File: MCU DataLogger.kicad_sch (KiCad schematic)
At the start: 0 parts

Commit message: Symbols added to first and second sheet
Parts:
- added BT1: Battery, symbol Device:Battery
- added C1, C2, C3, C4: C, symbol Device:C
- added C5: C_Polarized, symbol Device:C_Polarized
- added D1, D2: LED, symbol Device:LED
- added H1, H2, H3, H4: MountingHole, symbol Mechanical:MountingHole
- added R1, R2, R3, R4, R5, R6, R7: R, symbol Device:R
- added U1, U2: 24LC1025, symbol Memory_EEPROM:24LC1025
- added U3: DS1337S_, DS1337S_:SOIC127P600X175-8N, symbol DS1337S_:DS1337S_
- added U4: ATMEGA328P-AU, ATMEGA328P-AU:QFP80P900X900X120-32N, symbol ATMEGA328P-AU:ATMEGA328P-AU
- added Y1: Crystal, symbol Device:Crystal
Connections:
- new net GND: U4.21 (GND), U4.3 (GND), U4.5 (GND)
- new net VCC: U4.4 (VCC), U4.6 (VCC)
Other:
- added sheet Connectors (Connectors.kicad_sch)
- title: (none) -> ${project_name}

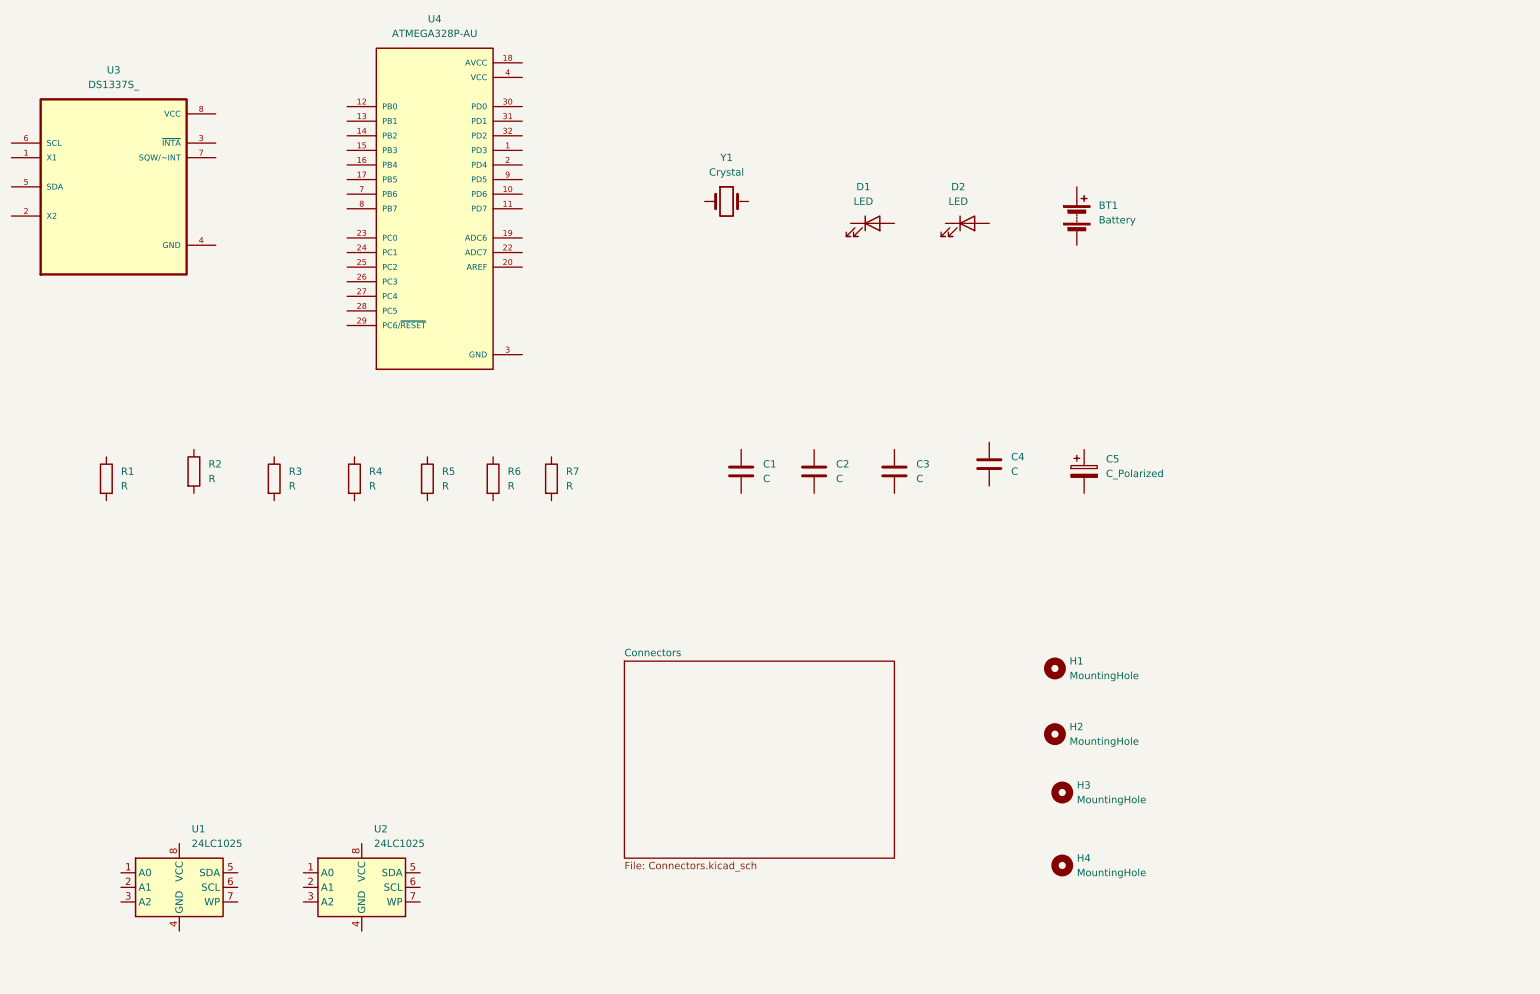
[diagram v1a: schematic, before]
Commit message: Symbols arranged pre annonation
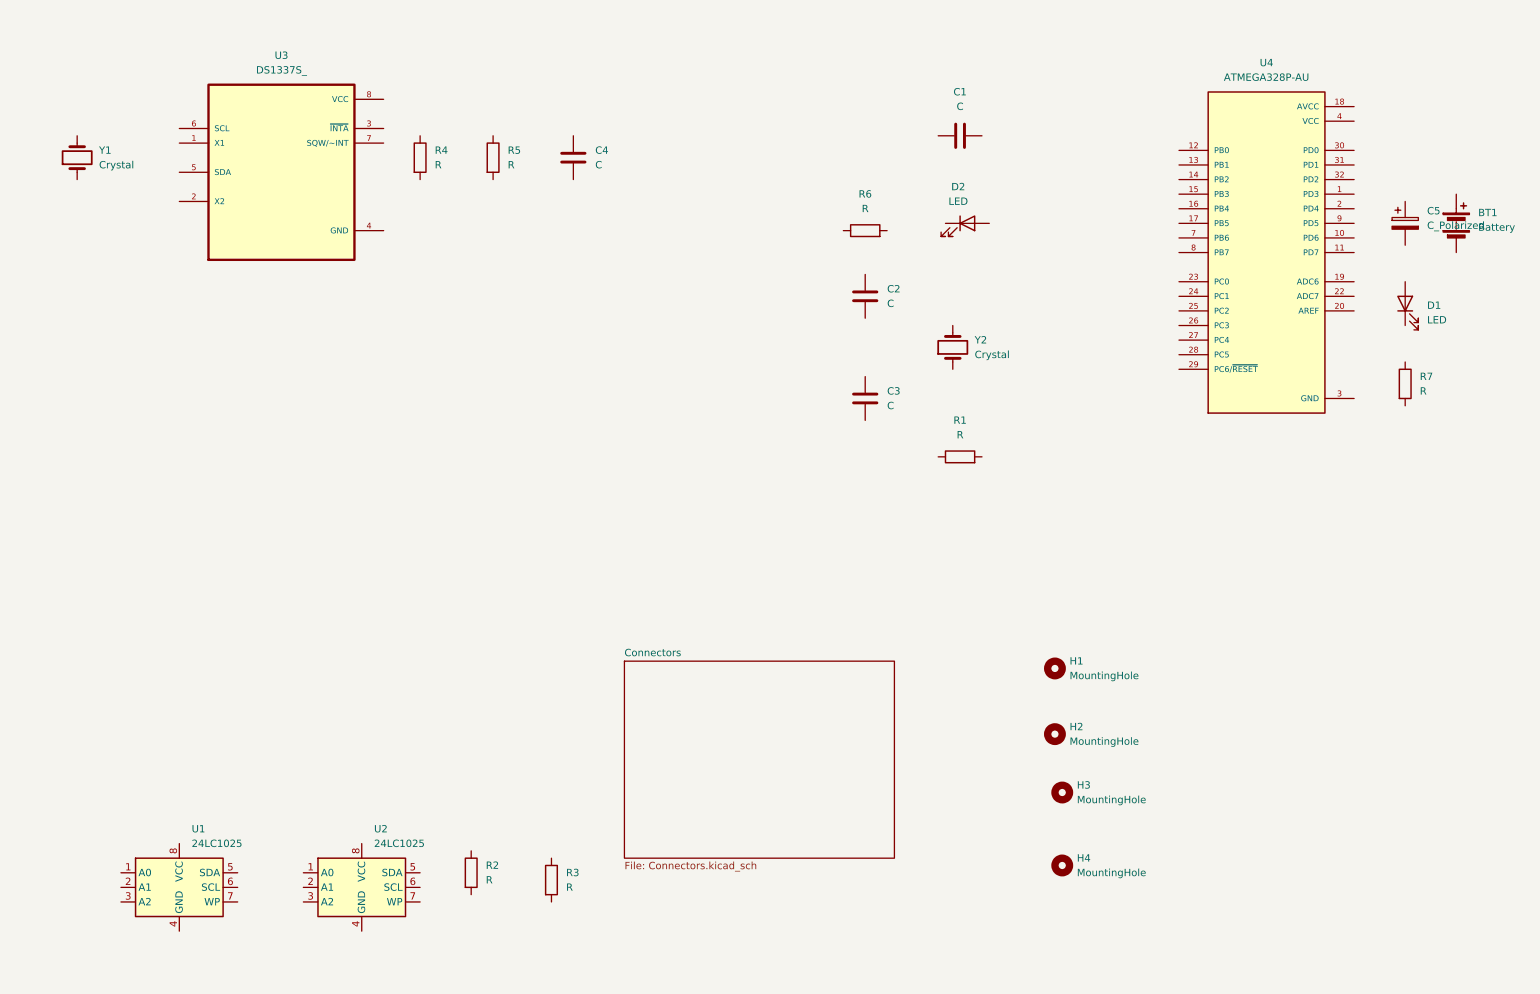
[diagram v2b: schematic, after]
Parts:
- added Y2: Crystal, symbol Device:Crystal
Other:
- moved on the sheet: BT1, C1, C2, C3, C4, C5, D1, R1, R2, R3, R4, R5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

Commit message: Symbols annotated with componenet values
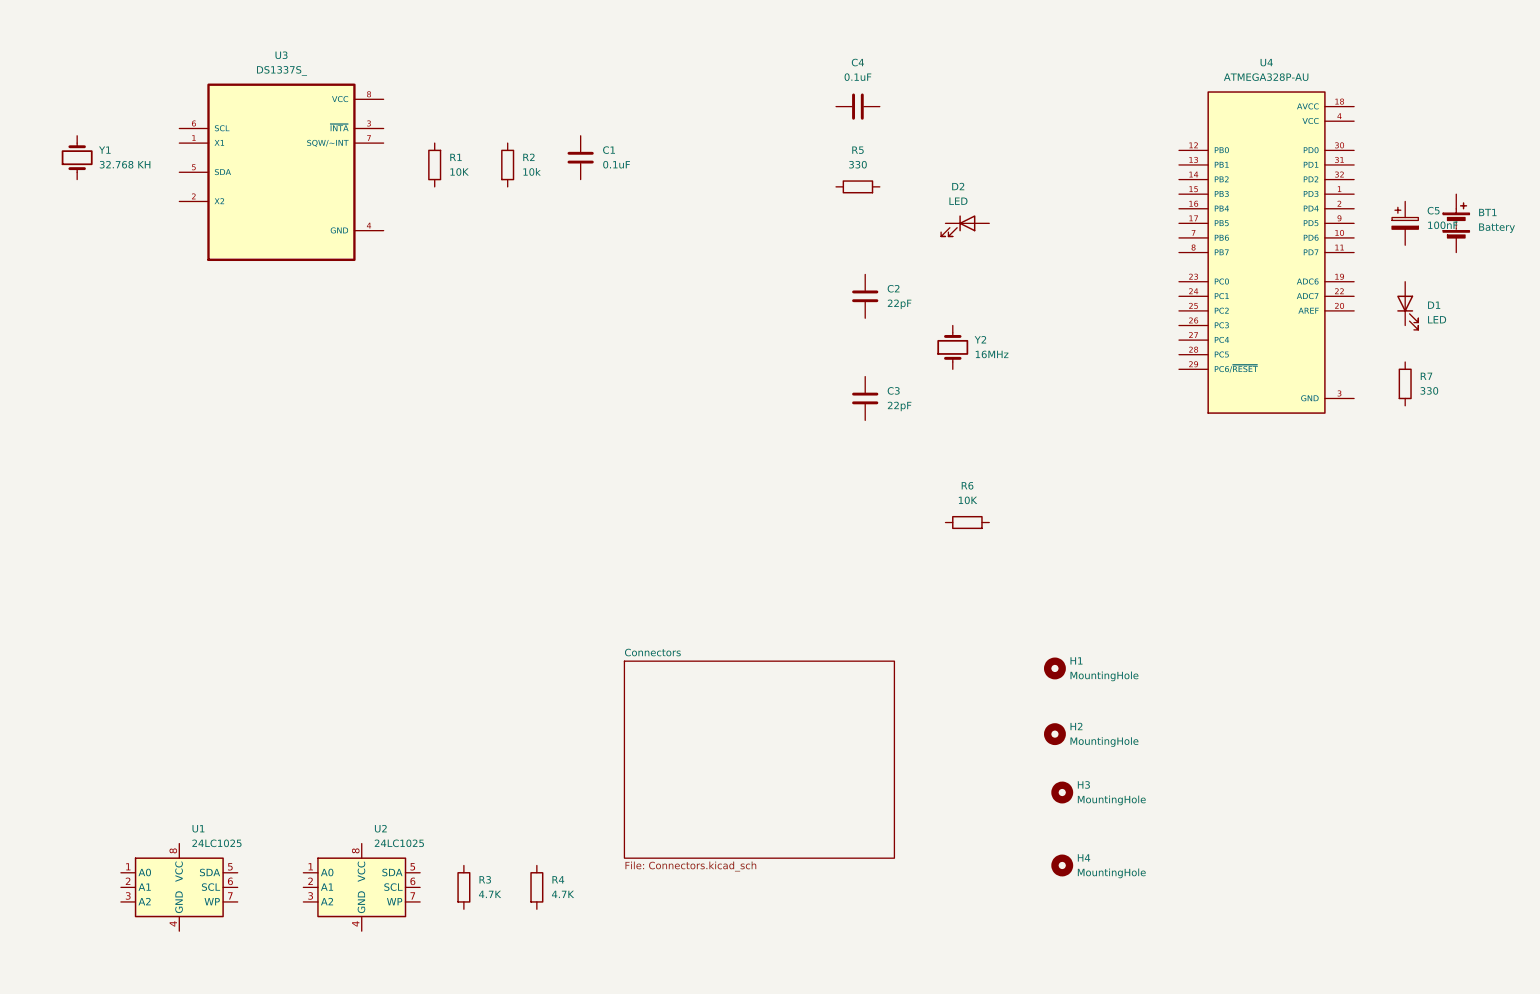
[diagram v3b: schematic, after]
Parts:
- C1, C4: value C -> 0.1uF
- C2, C3: value C -> 22pF
- C5: value C_Polarized -> 100nF
- R1, R6: value R -> 10K
- R2: value R -> 10k
- R3, R4: value R -> 4.7K
- R5, R7: value R -> 330
- Y1: value Crystal -> 32.768 KH
- Y2: value Crystal -> 16MHz
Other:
- moved on the sheet: C1, C4, R1, R2, R3, R4, R5, R6

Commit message: Added footprints to most of the symbols
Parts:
- BT1: footprint (none) -> Connector_PinHeader_2.54mm:PinHeader_1x02_P2.54mm_Vertical
- C1, C2, C3, C4, C5: footprint (none) -> Capacitor_SMD:C_0805_2012Metric
- D1, D2: footprint (none) -> LED_SMD:LED_0805_2012Metric
- H1, H2, H3, H4: footprint (none) -> MountingHole:MountingHole_2.1mm
- R1, R2, R3, R4, R5, R6, R7: footprint (none) -> Resistor_SMD:R_0805_2012Metric
- U3: footprint DS1337S_:SOIC127P600X175-8N -> Footprints:SOIC127P600X175-8N
- U4: footprint ATMEGA328P-AU:QFP80P900X900X120-32N -> Footprints:QFP80P900X900X120-32N
- Y1: footprint (none) -> Crystal:Crystal_SMD_5032-2Pin_5.0x3.2mm
- Y2: footprint (none) -> Crystal:Crystal_SMD_5032-2Pin_5.0x3.2mm_HandSoldering
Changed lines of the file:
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@@
 			)
 		)
-		(property "Footprint" ""
+		(property "Footprint" "LED_SMD:LED_0805_2012Metric"
 			(at 186.69 49.53 0)
 			(hide yes)
@@
 			)
 		)
-		(property "Footprint" ""
+		(property "Footprint" "MountingHole:MountingHole_2.1mm"
 			(at 201.93 127 0)
 			(hide yes)
@@
 			)
 		)
-		(property "Footprint" ""
+		(property "Footprint" "Resistor_SMD:R_0805_2012Metric"
 			(at 109.982 165.1 90)
 			(hide yes)
@@
 			)
 		)
-		(property "Footprint" "DS1337S_:SOIC127P600X175-8N"
+		(property "Footprint" "Footprints:SOIC127P600X175-8N"
 			(at 67.31 40.64 0)
 			(hide yes)
@@
 			)
 		)
-		(property "Footprint" ""
+		(property "Footprint" "Crystal:Crystal_SMD_5032-2Pin_5.0x3.2mm_HandSoldering"
 			(at 184.15 71.12 0)
 			(hide yes)
@@
 			)
 		)
-		(property "Footprint" ""
+		(property "Footprint" "MountingHole:MountingHole_2.1mm"
 			(at 201.93 138.43 0)
 			(hide yes)
@@
 			)
 		)
-		(property "Footprint" ""
+		(property "Footprint" "Capacitor_SMD:C_0805_2012Metric"
 			(at 169.8752 66.04 0)
 			(hide yes)
@@
 			)
 		)
-		(property "Footprint" ""
+		(property "Footprint" "Resistor_SMD:R_0805_2012Metric"
 			(at 167.64 44.958 90)
 			(hide yes)
@@
 			)
 		)
-		(property "Footprint" ""
+		(property "Footprint" "Resistor_SMD:R_0805_2012Metric"
 			(at 261.112 77.47 90)
 			(hide yes)
@@
 			)
 		)
-		(property "Footprint" ""
+		(property "Footprint" "Capacitor_SMD:C_0805_2012Metric"
 			(at 263.8552 53.34 0)
 			(hide yes)
@@
 			)
 		)
-		(property "Footprint" ""
+		(property "Footprint" "Resistor_SMD:R_0805_2012Metric"
 			(at 104.902 39.37 90)
 			(hide yes)
@@
 			)
 		)
-		(property "Footprint" ""
+		(property "Footprint" "Crystal:Crystal_SMD_5032-2Pin_5.0x3.2mm"
 			(at 31.75 38.1 0)
 			(hide yes)
@@
 			)
 		)
-		(property "Footprint" "ATMEGA328P-AU:QFP80P900X900X120-32N"
+		(property "Footprint" "Footprints:QFP80P900X900X120-32N"
 			(at 238.76 54.61 0)
 			(hide yes)
@@
 			)
 		)
-		(property "Footprint" ""
+		(property "Footprint" "MountingHole:MountingHole_2.1mm"
 			(at 203.2 161.29 0)
 			(hide yes)
@@
 			)
 		)
-		(property "Footprint" ""
+		(property "Footprint" "LED_SMD:LED_0805_2012Metric"
 			(at 262.89 63.5 0)
 			(hide yes)
@@
 			)
 		)
-		(property "Footprint" ""
+		(property "Footprint" "Capacitor_SMD:C_0805_2012Metric"
 			(at 118.4148 34.29 0)
 			(hide yes)
@@
 			)
 		)
-		(property "Footprint" ""
+		(property "Footprint" "Resistor_SMD:R_0805_2012Metric"
 			(at 97.282 165.1 90)
 			(hide yes)
@@
 			)
 		)
-		(property "Footprint" ""
+		(property "Footprint" "MountingHole:MountingHole_2.1mm"
 			(at 203.2 148.59 0)
 			(hide yes)
@@
 			)
 		)
-		(property "Footprint" ""
+		(property "Footprint" "Resistor_SMD:R_0805_2012Metric"
 			(at 95.758 39.37 90)
 			(hide yes)
@@
 			)
 		)
-		(property "Footprint" ""
+		(property "Footprint" "Capacitor_SMD:C_0805_2012Metric"
 			(at 171.45 28.2448 0)
 			(hide yes)
@@
 			)
 		)
-		(property "Footprint" ""
+		(property "Footprint" "Connector_PinHeader_2.54mm:PinHeader_1x02_P2.54mm_Vertical"
 			(at 271.78 48.006 90)
 			(hide yes)
@@
 			)
 		)
-		(property "Footprint" ""
+		(property "Footprint" "Capacitor_SMD:C_0805_2012Metric"
 			(at 169.8752 83.82 0)
 			(hide yes)
@@
 			)
 		)
-		(property "Footprint" ""
+		(property "Footprint" "Resistor_SMD:R_0805_2012Metric"
 			(at 186.69 103.378 90)
 			(hide yes)

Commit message: Sheet one wired
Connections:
- net GND: now also BT1.2 (-), C1.1, C2.1, C3.1, C4.1, C5.2, R5.1, R7.2, U1.4 (GND), U1.7 (WP), U2.2 (A1), U2.4 (GND), U2.7 (WP), U3.4 (GND)
- net at D2.1 (K): now also R5.2
- net SCK: now reaches D2.2 (A)
- net SCK: now also R3.2, U1.6 (SCL), U2.6 (SCL), U3.6 (SCL), U4.17 (PB5), U4.28 (PC5)
- net Vcc: now reaches R4.1
- net Vcc: now also R3.1, R6.1, U1.1 (A0), U1.2 (A1), U1.3 (A2), U1.8 (VCC), U2.1 (A0), U2.3 (A2), U2.8 (VCC)
- net SDA: now reaches R4.2
- net SDA: now also U1.5 (SDA), U2.5 (SDA), U3.5 (SDA), U4.27 (PC4)
- net at U3.1 (X1): now also Y1.2
- net at U3.2 (X2): now also Y1.1
- net at U3.3 (~{INTA}): now also R1.1
- net at U3.7 (SQW/~INT): now also R2.2
- net at U3.8 (VCC): now also C1.2, R1.2, R2.1
- net at Y2.1: now also C3.2, U4.8 (PB7)
- net at Y2.2: now also C2.2, U4.7 (PB6)
- net at R7.1: now also D1.1 (K)
- net at C5.1: now also BT1.1 (+), D1.2 (A), U4.18 (AVCC), U4.4 (VCC)
- net D3: now reaches U4.1 (PD3)
- net D6: now reaches U4.10 (PD6)
- net D7: now reaches U4.11 (PD7)
- net D8: now reaches U4.12 (PB0)
- net MOSI: now reaches U4.15 (PB3)
- net MISO: now reaches U4.16 (PB4)
- net D4: now reaches U4.2 (PD4)
- net at U4.20 (AREF): now also C4.2
- net RESET: now reaches U4.29 (PC6/~{RESET})
- net RESET: now also R6.2
- net RX: now reaches U4.30 (PD0)
- net TX: now reaches U4.31 (PD1)
- net D2: now reaches U4.32 (PD2)
- net D5: now reaches U4.9 (PD5)
- net VCC: no longer names the net of U4.6 (VCC)
- net VCC: no longer U4.4 (VCC)
- no-connect marks 0 -> 9
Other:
- moved on the sheet: BT1, C2, C3, C4, C5, D1, D2, R1, R2, R5, R6, R7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
